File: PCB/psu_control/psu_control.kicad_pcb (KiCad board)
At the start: 4 copper layers, 100 x 70 mm, 125 parts, among them J1 Vin (10-25V), J11 Light Sensor Front, J12 Light Sensor Left, J13 Light Sensor Back, J14 Light Sensor Right, J15 RRC-PMM240, J16 RS232, J2 Vout (10-25V), J4 Vout (10-25V), J6 LED Strip, J7 Amplifier 2 I2C, J8 Amplifier 1 I2C, M1 Fan, M2 Fan, Q1 SSM3J372R, Q2 IPD068P03L3GATMA1, Q3 T2N7002AK, Q4 DMG9926USD, SW1 Non-Momentary DPST, SW2 BUTTON, SW3 BUTTON, SW4 BUTTON, SW5 BUTTON, SW6 BUTTON, U1 LM810M3-4.63, U2 Teensy_LC, U3 INA220, U4 K7805-3AR3, U5 74HC14, U6 SN74LV1T34, U7 SN65C3221E, U8 74LVC2G34

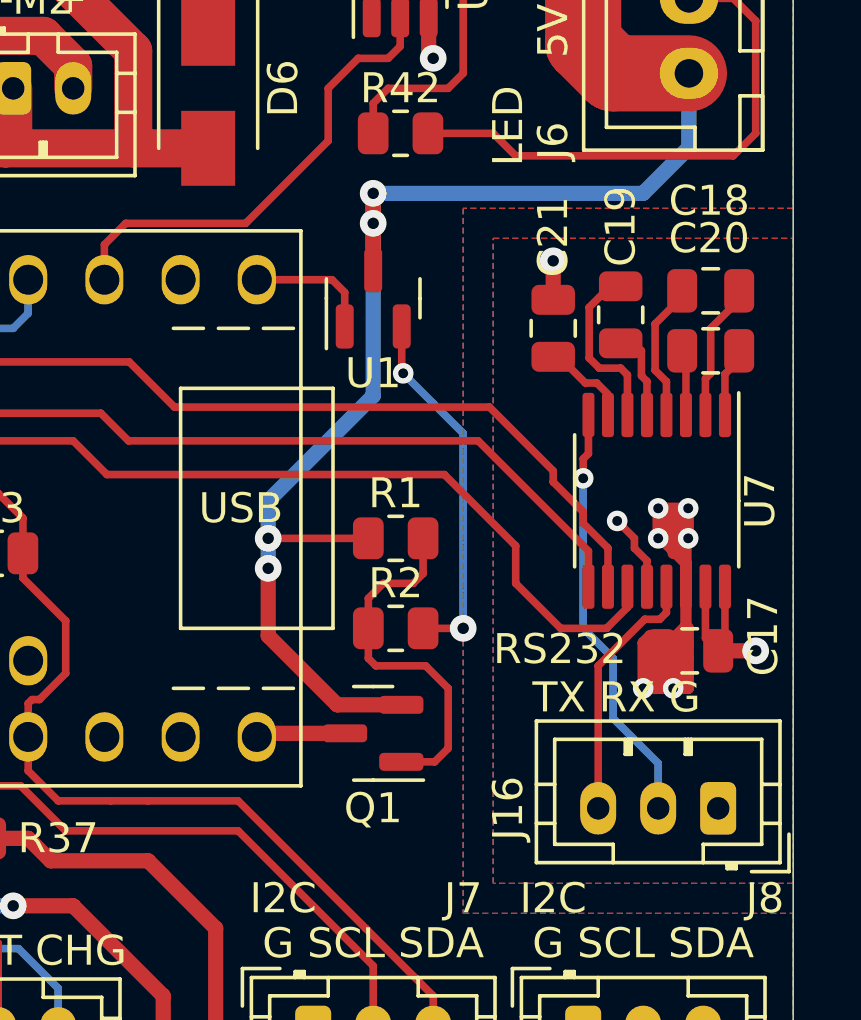
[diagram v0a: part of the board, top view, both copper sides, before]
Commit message: Remove voltage supervisors
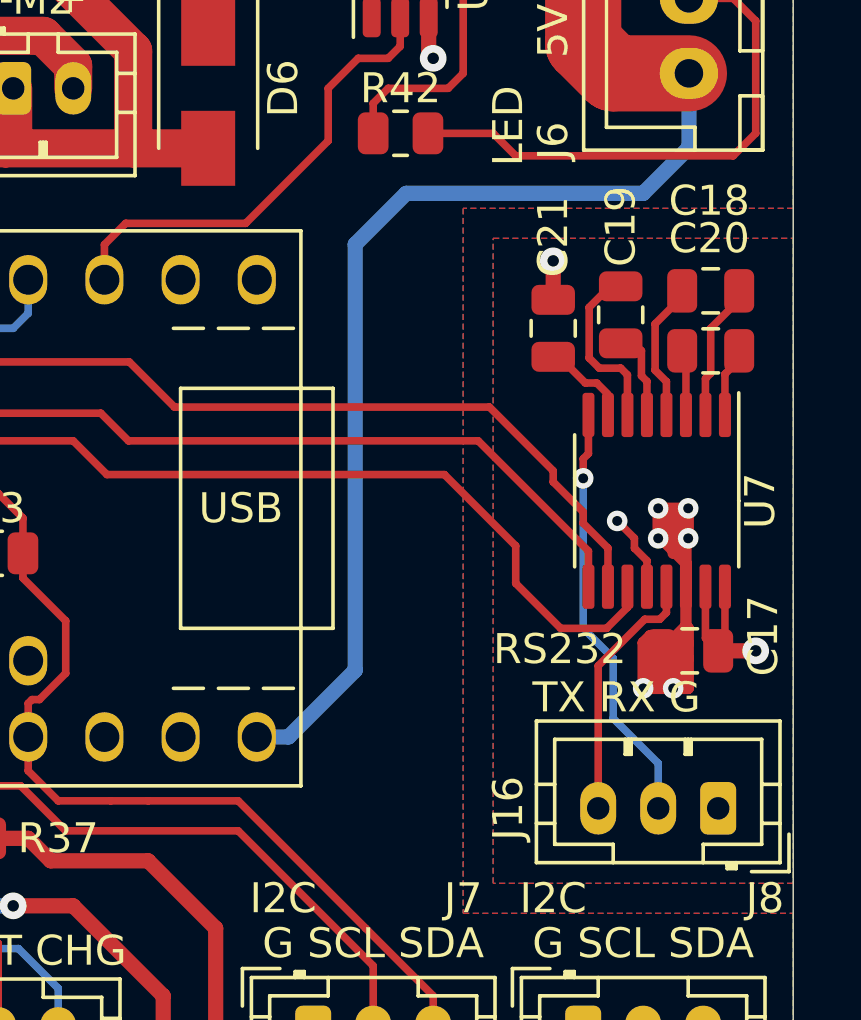
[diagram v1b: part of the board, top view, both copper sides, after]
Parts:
- removed Q1: SSM3J372R, Package_TO_SOT_SMD:SOT-23
- removed R1: 100k, Resistor_SMD:R_0805_2012Metric
- removed R2: 511, Resistor_SMD:R_0805_2012Metric
- removed U1: LM810M3-4.63, Package_TO_SOT_SMD:SOT-23
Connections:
- U2 pad VIN: Net-(Q1-Pad3) -> +5V
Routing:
- net Net-(R2-Pad1): track 12.2 -> 0.00 mm, vias 2 -> 0
- net Net-(Q1-Pad1): track 12.2 -> 0.00 mm
- net +5V: track 127.9 -> 120.1 mm, vias 4 -> 0
- net GND: track 100.5 -> 96.2 mm
- net Net-(Q1-Pad3): track 2.99 -> 0.00 mm

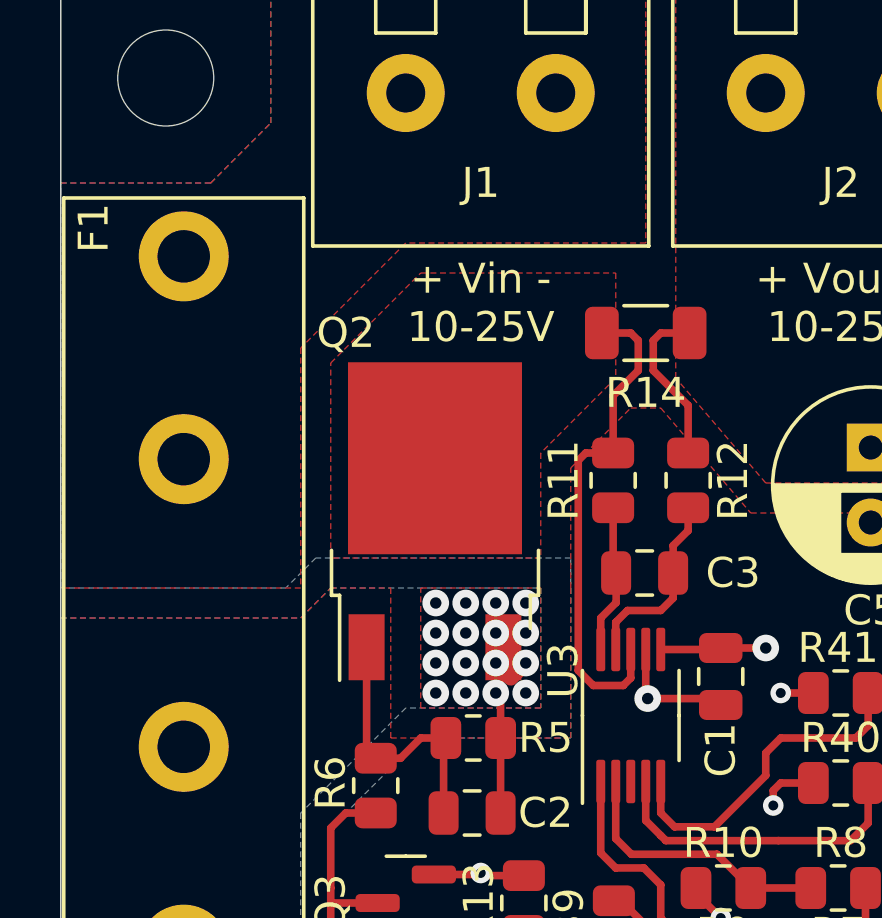
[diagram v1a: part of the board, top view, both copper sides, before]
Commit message: Fix the psu_control PCB.
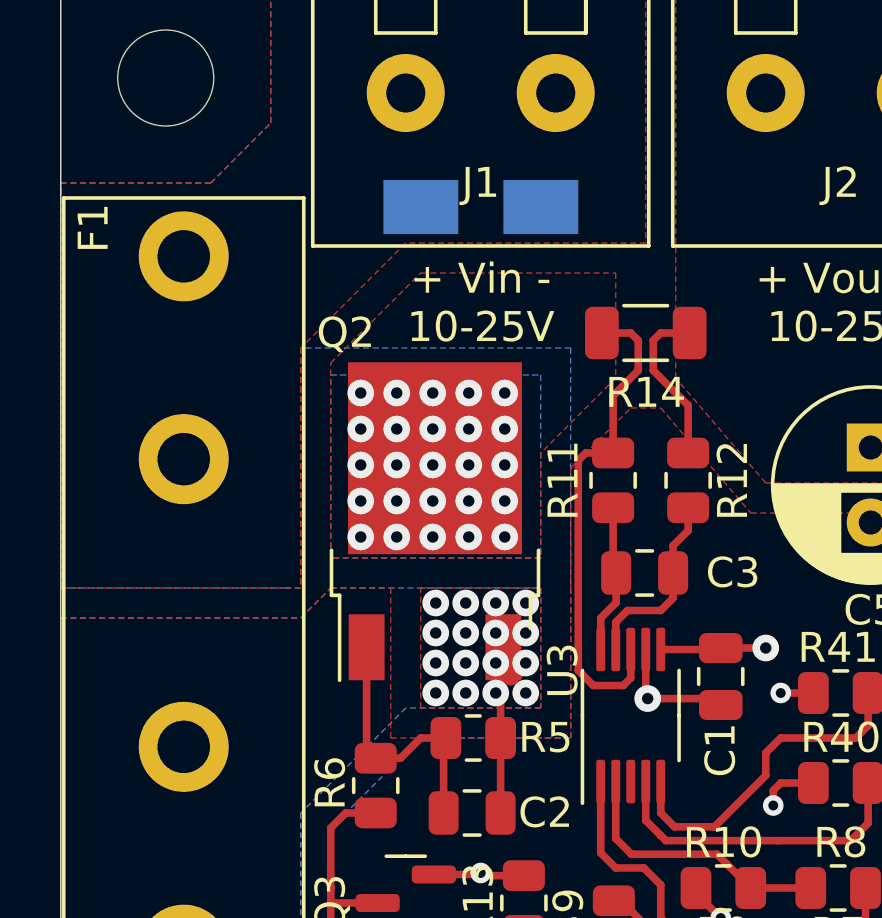
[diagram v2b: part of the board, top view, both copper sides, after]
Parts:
- added D7: SZ1SMA24AT3G, Diode_SMD:D_SMA, B.Cu at (29.0, 22.8)
- C2: value 2.2µF/25V -> 22µF/25V
- Q2: value IPD068P03L3GATMA1 -> SUD50P04-09L-E3
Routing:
- net Net-(Q2-Pad2): vias 0 -> 25
- added copper zone on B.Cu, net Net-(Q2-Pad2)
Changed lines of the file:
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@@
       (effects (font (size 1 1) (thickness 0.15)))
     )
-    (fp_text value "2.2µF/25V" (at 0 1.68) (layer "F.Fab")
+    (fp_text value "22µF/25V" (at 0 1.68) (layer "F.Fab")
       (effects (font (size 1 1) (thickness 0.15)))
     )
@@
       (effects (font (size 1 1) (thickness 0.15)))
     )
-    (fp_text value "IPD068P03L3GATMA1" (at 0 4.5 90) (layer "F.Fab")
+    (fp_text value "SUD50P04-09L-E3" (at 0 4.5 90) (layer "F.Fab")
       (effects (font (size 1 1) (thickness 0.15)))
     )
@@
     )
   )
+  (footprint "Diode_SMD:D_SMA" (layer "B.Cu")
+    (at 29 22.8)
+    (descr "Diode SMA (DO-214AC)")
+    (tags "Diode SMA (DO-214AC)")
+    (property "Sheetfile" "power.kicad_sch")
+    (property "Sheetname" "Power")
+    (attr smd)
+    (fp_text reference "D7" (at 0 2.5) (layer "B.SilkS")
+      (effects (font (size 1 1) (thickness 0.15)) (justify mirror))
+    )
+    (fp_text value "SZ1SMA24AT3G" (at 0 -2.6) (layer "B.Fab")
+      (effects (font (size 1 1) (thickness 0.15)) (justify mirror))
+    )
+    (fp_text user "${REFERENCE}" (at 0 2.5) (layer "B.Fab")
+      (effects (font (size 1 1) (thickness 0.15)) (justify mirror))
+    )
+    (fp_line (start -3.4 -1.65) (end 2 -1.65) (layer "B.SilkS") (width 0.12))
+    (fp_line (start -3.4 1.65) (end -3.4 -1.65) (layer "B.SilkS") (width 0.12))
+    (fp_line (start -3.4 1.65) (end 2 1.65) (layer "B.SilkS") (width 0.12))
+    (fp_line (start -3.5 1.75) (end 3.5 1.75) (layer "B.CrtYd") (width 0.05))
+    (fp_line (start -3.5 -1.75) (end -3.5 1.75) (layer "B.CrtYd") (width 0.05))
+    (fp_line (start 3.5 -1.75) (end -3.5 -1.75) (layer "B.CrtYd") (width 0.05))
+    (fp_line (start 3.5 1.75) (end 3.5 -1.75) (layer "B.CrtYd") (width 0.05))
+    (fp_line (start -0.64944 0.79908) (end -0.64944 -0.80112) (layer "B.Fab") (width 0.1))
+    (fp_line (start 2.3 1.5) (end -2.3 1.5) (layer "B.Fab") (width 0.1))
+    (fp_line (start 0.50118 -0.00102) (end 1.4994 -0.00102) (layer "B.Fab") (width 0.1))
+    (fp_line (start -0.64944 -0.00102) (end 0.50118 0.79908) (layer "B.Fab") (width 0.1))
+    (fp_line (start 0.50118 -0.75032) (end 0.50118 0.79908) (layer "B.Fab") (width 0.1))
+    (fp_line (start -0.64944 -0.00102) (end 0.50118 -0.75032) (layer "B.Fab") (width 0.1))
+    (fp_line (start 2.3 1.5) (end 2.3 -1.5) (layer "B.Fab") (width 0.1))
+    (fp_line (start 2.3 -1.5) (end -2.3 -1.5) (layer "B.Fab") (width 0.1))
+    (fp_line (start -2.3 -1.5) (end -2.3 1.5) (layer "B.Fab") (width 0.1))
+    (fp_line (start -0.64944 -0.00102) (end -1.55114 -0.00102) (layer "B.Fab") (width 0.1))
+    (pad "1" smd rect (at -2 0) (size 2.5 1.8) (layers "B.Cu" "B.Paste" "B.Mask")
+      (net 27 "Net-(F1-Pad1)") (pinfunction "K") (pintype "passive"))
+    (pad "2" smd rect (at 2 0) (size 2.5 1.8) (layers "B.Cu" "B.Paste" "B.Mask")
+      (net 2 "GND") (pinfunction "A") (pintype "passive"))
+    (model "${KICAD6_3DMODEL_DIR}/Diode_SMD.3dshapes/D_SMA.wrl"
+      (offset (xyz 0 0 0))
+      (scale (xyz 1 1 1))
+      (rotate (xyz 0 0 0))
+    )
+  )
   (footprint "Resistor_SMD:R_0805_2012Metric" (layer "B.Cu")
     (at 94.5875 21)
@@
   (segment (start 34 38.5) (end 34 37.55) (width 0.254) (layer "F.Cu") (net 72))
   (segment (start 34.25 28.25) (end 33.4125 29.0875) (width 0.254) (layer "F.Cu") (net 72))
+  (via (at 25 33.8) (size 0.889) (drill 0.381) (layers "F.Cu" "B.Cu") (net 72))
+  (via (at 29.8 29) (size 0.889) (drill 0.381) (layers "F.Cu" "B.Cu") (net 72))
+  (via (at 28.6 31.4) (size 0.889) (drill 0.381) (layers "F.Cu" "B.Cu") (net 72))
+  (via (at 28.6 33.8) (size 0.889) (drill 0.381) (layers "F.Cu" "B.Cu") (net 72))
+  (via (at 29.8 30.2) (size 0.889) (drill 0.381) (layers "F.Cu" "B.Cu") (net 72))
+  (via (at 26.2 32.6) (size 0.889) (drill 0.381) (layers "F.Cu" "B.Cu") (net 72))
+  (via (at 28.6 30.2) (size 0.889) (drill 0.381) (layers "F.Cu" "B.Cu") (net 72))
+  (via (at 25 32.6) (size 0.889) (drill 0.381) (layers "F.Cu" "B.Cu") (net 72))
+  (via (at 29.8 31.4) (size 0.889) (drill 0.381) (layers "F.Cu" "B.Cu") (net 72))
+  (via (at 27.4 30.2) (size 0.889) (drill 0.381) (layers "F.Cu" "B.Cu") (net 72))
+  (via (at 26.2 29) (size 0.889) (drill 0.381) (layers "F.Cu" "B.Cu") (net 72))
+  (via (at 28.6 29) (size 0.889) (drill 0.381) (layers "F.Cu" "B.Cu") (net 72))
+  (via (at 26.2 30.2) (size 0.889) (drill 0.381) (layers "F.Cu" "B.Cu") (net 72))
+  (via (at 29.8 33.8) (size 0.889) (drill 0.381) (layers "F.Cu" "B.Cu") (net 72))
+  (via (at 27.4 29) (size 0.889) (drill 0.381) (layers "F.Cu" "B.Cu") (net 72))
+  (via (at 26.2 31.4) (size 0.889) (drill 0.381) (layers "F.Cu" "B.Cu") (net 72))
+  (via (at 25 31.4) (size 0.889) (drill 0.381) (layers "F.Cu" "B.Cu") (net 72))
+  (via (at 29.8 32.6) (size 0.889) (drill 0.381) (layers "F.Cu" "B.Cu") (net 72))
+  (via (at 25 29) (size 0.889) (drill 0.381) (layers "F.Cu" "B.Cu") (net 72))
+  (via (at 27.4 32.6) (size 0.889) (drill 0.381) (layers "F.Cu" "B.Cu") (net 72))
+  (via (at 26.2 33.8) (size 0.889) (drill 0.381) (layers "F.Cu" "B.Cu") (net 72))
+  (via (at 28.6 32.6) (size 0.889) (drill 0.381) (layers "F.Cu" "B.Cu") (net 72))
+  (via (at 27.4 31.4) (size 0.889) (drill 0.381) (layers "F.Cu" "B.Cu") (net 72))
+  (via (at 27.4 33.8) (size 0.889) (drill 0.381) (layers "F.Cu" "B.Cu") (net 72))
+  (via (at 25 30.2) (size 0.889) (drill 0.381) (layers "F.Cu" "B.Cu") (net 72))
   (segment (start 86.425 65.925) (end 85.75 65.25) (width 0.254) (layer "F.Cu") (net 73))
   (segment (start 76.007533 60.202467) (end 76.05 60.16) (width 0.254) (layer "F.Cu") (net 73))
@@
     )
   )
+  (zone (net 72) (net_name "Net-(Q2-Pad2)") (layer "B.Cu") (hatch edge 0.508)
+    (connect_pads (clearance 0.508))
+    (min_thickness 0.254) (filled_areas_thickness no)
+    (fill yes (thermal_gap 0.508) (thermal_bridge_width 0.508))
+    (polygon
+      (pts
+        (xy 31 34.5)
+        (xy 24 34.5)
+        (xy 24 28.4)
+        (xy 31 28.4)
+      )
+    )
+  )
   (zone (net 2) (net_name "GND") (layer "B.Cu") (hatch edge 0.508)
     (connect_pads yes (clearance 0.508))
@@
         (xy 27 40.5)
         (xy 32 40.5)
-        (xy 32 34.5)
-        (xy 23.5 34.5)
+        (xy 32 27.5)
+        (xy 23 27.5)
+        (xy 23 35.5)
         (xy 22.5 35.5)
         (xy 15 35.5)

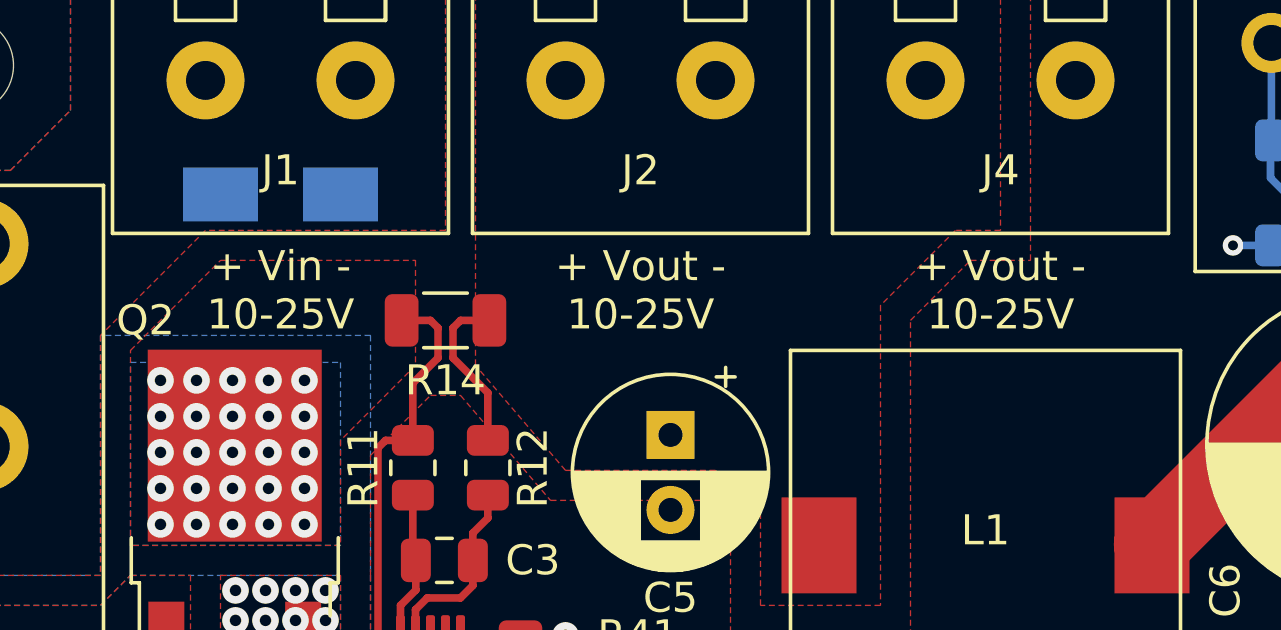
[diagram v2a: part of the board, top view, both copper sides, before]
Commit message: Fix the max input voltage in the psu_control PCB.
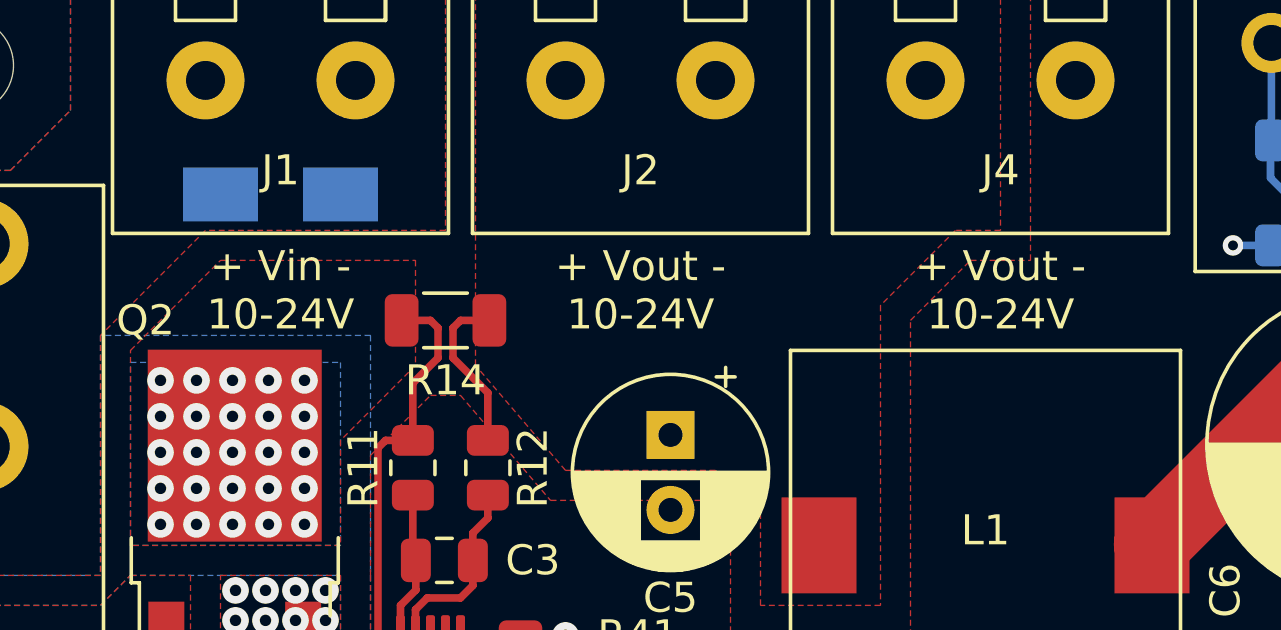
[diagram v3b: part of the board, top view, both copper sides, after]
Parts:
- J1: value Vin (10-25V) -> Vin (10-24V)
- J2, J4: value Vout (10-25V) -> Vout (10-24V)
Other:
- board text added: "+ Vin - 10-24V"
- board text added: "+ Vout - 10-24V"
- board text removed: "+ Vin - 10-25V"
- board text removed: "+ Vout - 10-25V"
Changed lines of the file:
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@@
   (net 25 "Net-(D4-Pad2)")
   (net 26 "Net-(D5-Pad2)")
-  (net 27 "Net-(F1-Pad1)")
+  (net 27 "Net-(D7-Pad1)")
   (net 28 "Net-(J6-Pad2)")
   (net 29 "/GENERAL_SCL")
@@
       (effects (font (size 1 1) (thickness 0.15)))
     )
-    (fp_text value "Vout (10-25V)" (at 0 -2.5) (layer "F.Fab")
+    (fp_text value "Vout (10-24V)" (at 0 -2.5) (layer "F.Fab")
       (effects (font (size 1 1) (thickness 0.15)))
     )
@@
       (effects (font (size 1 1) (thickness 0.15)))
     )
-    (fp_text value "Vout (10-25V)" (at 0 -2.5) (layer "F.Fab")
+    (fp_text value "Vout (10-24V)" (at 0 -2.5) (layer "F.Fab")
       (effects (font (size 1 1) (thickness 0.15)))
     )
@@
       (effects (font (size 1 1) (thickness 0.15)))
     )
-    (fp_text value "Vin (10-25V)" (at 0 -2.5) (layer "F.Fab")
+    (fp_text value "Vin (10-24V)" (at 0 -2.5) (layer "F.Fab")
       (effects (font (size 1 1) (thickness 0.15)))
     )
@@
       (net 2 "GND") (pinfunction "Pin_1") (pintype "passive"))
     (pad "2" thru_hole circle locked (at 2.5 0 180) (size 2.6 2.6) (drill 1.3) (layers *.Cu *.Mask)
-      (net 27 "Net-(F1-Pad1)") (pinfunction "Pin_2") (pintype "passive"))
+      (net 27 "Net-(D7-Pad1)") (pinfunction "Pin_2") (pintype "passive"))
   )
   (footprint "Resistor_SMD:R_0805_2012Metric" (layer "F.Cu")
@@
     (fp_line (start -13.5 -4) (end 13.5 -4) (layer "F.SilkS") (width 0.12))
     (pad "1" thru_hole circle locked (at -11.555 0 270) (size 3 3) (drill 1.75) (layers *.Cu *.Mask)
-      (net 27 "Net-(F1-Pad1)") (pintype "passive"))
+      (net 27 "Net-(D7-Pad1)") (pintype "passive"))
     (pad "1" thru_hole circle locked (at -4.795 0 270) (size 3 3) (drill 1.75) (layers *.Cu *.Mask)
-      (net 27 "Net-(F1-Pad1)") (pintype "passive"))
+      (net 27 "Net-(D7-Pad1)") (pintype "passive"))
     (pad "2" thru_hole circle locked (at 4.795 0 270) (size 3 3) (drill 1.75) (layers *.Cu *.Mask)
       (net 3 "Net-(C2-Pad1)") (pintype "passive"))
@@
     (fp_line (start -0.64944 -0.00102) (end -1.55114 -0.00102) (layer "B.Fab") (width 0.1))
     (pad "1" smd rect (at -2 0) (size 2.5 1.8) (layers "B.Cu" "B.Paste" "B.Mask")
-      (net 27 "Net-(F1-Pad1)") (pinfunction "K") (pintype "passive"))
+      (net 27 "Net-(D7-Pad1)") (pinfunction "K") (pintype "passive"))
     (pad "2" smd rect (at 2 0) (size 2.5 1.8) (layers "B.Cu" "B.Paste" "B.Mask")
       (net 2 "GND") (pinfunction "A") (pintype "passive"))
@@
   (gr_line (start 15 15) (end 15 55) (layer "Edge.Cuts") (width 0.05))
   (gr_line (start 115 15) (end 115 85) (layer "Edge.Cuts") (width 0.05))
-  (gr_text "+ Vin -\n10-25V" (at 29 26) (layer "F.SilkS")
+  (gr_text "+ Vin -\n10-24V" (at 29 26) (layer "F.SilkS")
     (effects (font (size 1 1) (thickness 0.15)))
   )
@@
     (effects (font (size 1 1) (thickness 0.15)))
   )
-  (gr_text "+ Vout -\n10-25V" (at 41 26) (layer "F.SilkS")
+  (gr_text "+ Vout -\n10-24V" (at 41 26) (layer "F.SilkS")
     (effects (font (size 1 1) (thickness 0.15)))
   )
@@
     (effects (font (size 1 1) (thickness 0.15)))
   )
-  (gr_text "+ Vout -\n10-25V" (at 53 26) (layer "F.SilkS")
+  (gr_text "+ Vout -\n10-24V" (at 53 26) (layer "F.SilkS")
     (effects (font (size 1 1) (thickness 0.15)))
   )
@@
     )
   )
-  (zone (net 27) (net_name "Net-(F1-Pad1)") (layer "F.Cu") (hatch edge 0.508)
+  (zone (net 27) (net_name "Net-(D7-Pad1)") (layer "F.Cu") (hatch edge 0.508)
     (connect_pads yes (clearance 0.508))
     (min_thickness 0.254) (filled_areas_thickness no)
